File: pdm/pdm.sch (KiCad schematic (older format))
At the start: 29 parts, among them J1 Conn_01x05, J2 Conn_01x04_Male, SW1 SW_Push, U1 AZ1117CH-3_3TRG1, U2 SN65HVD233, U3 STM32F042G6Ux

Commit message: changed to molex headers
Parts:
- removed H6, H7: MountingHole_Pad, MountingHole:MountingHole_4mm_Pad_Via, symbol Mechanical:MountingHole_Pad
- removed J1: Conn_01x05, Connector_PinHeader_2.00mm:PinHeader_1x05_P2.00mm_Vertical, symbol Connector_Generic:Conn_01x05
- removed J2: Conn_01x04_Male, Connector_PinHeader_2.00mm:PinHeader_1x04_P2.00mm_Horizontal, symbol Connector:Conn_01x04_Male
- added CANH_Test1: CANH_TEST, TestPoint:TestPoint_Pad_D1.0mm, symbol Connector:TestPoint_Probe
- added CANL_Test1: CANL_TEST, TestPoint:TestPoint_Pad_D1.0mm, symbol Connector:TestPoint_Probe
- added J1: Conn_01x04_Male, Connector_Molex:Molex_Mega-Fit_76829-0004_2x02_P5.70mm_Vertical, symbol Connector:Conn_01x04_Male
- added J2: Conn_01x08_Male, Connector_Molex:Molex_Mega-Fit_76829-0008_2x04_P5.70mm_Vertical, symbol Connector:Conn_01x08_Male
- added TP11, TP12, TP?: TestPoint_Probe, TestPoint:TestPoint_Pad_D1.0mm, symbol Connector:TestPoint_Probe
- C1: renamed from C9; value 100nF -> 0.1uF; Digi-Key_PN (none) -> CL21B104KBCNNNC
- C2: renamed from C3; value 0.1 uF -> 0.1uF; Digi-Key_PN (none) -> CL21B104KBCNNNC
- C3: renamed from C2; value 0.1 uF -> 0.1uF; Digi-Key_PN (none) -> CL21B104KBCNNNC
- C4: renamed from C6; value 20p -> 20pF; Digi-Key_PN (none) -> 08051A200JAT2A
- C5: renamed from C4; value 20p -> 20pF; Digi-Key_PN (none) -> 08051A200JAT2A
- C6: renamed from C1; footprint Capacitor_SMD:CP_Elec_4x5.4 -> Capacitor_Tantalum_SMD:CP_EIA-3216-18_Kemet-A_Pad1.58x1.35mm_HandSolder
- C7: renamed from C5; value 100nF -> 0.1uF; Digi-Key_PN (none) -> CL21B104KBCNNNC
- C8: renamed from C15; Digi-Key_PN (none) -> T494A106M020AT
- C9: renamed from C7; value 100nF -> 0.1uF; Digi-Key_PN (none) -> CL21B104KBCNNNC
- renumbered C14 to C10, C8 to C11, D11 to D1, D12 to D2, D1 to D3, R33 to R1, R1 to R2, R34 to R3, R2 to R4, R23 to R5, R24 to R6
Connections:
- wire segments 118 -> 131
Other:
- note added: "Signal Connector"
- note removed: "CAN Bus checkup? Is that alright?\n\nCANH and CANL - is the only criteria for differential the fact \nthey have to be close?"
- note removed: "Double Check the 12V Blocks"
- note removed: "General Questions"
- note removed: "SWD Programmer"
- note removed: "SWD Setup"
- note removed: "use an onboard connector - eg. use a pcb deutche\nconnector foor this one (DTM Connector)"
- moved on the sheet: C11, C3, C6, D1, D2, R1, R3, U1

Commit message: changed layout with two plugs
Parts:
- removed C1: 0.1uF, Capacitor_SMD:C_0805_2012Metric_Pad1.15x1.40mm_HandSolder, symbol Device:C
- removed J2: Conn_01x08_Male, Connector_Molex:Molex_Mega-Fit_76829-0008_2x04_P5.70mm_Vertical, symbol Connector:Conn_01x08_Male
- removed R2: 1M, Resistor_SMD:R_0805_2012Metric_Pad1.15x1.40mm_HandSolder, symbol Device:R
- added J2: Conn_01x12_Male, DT13-12PB-B016:TE_DT13-12PB-B016, symbol Connector:Conn_01x12_Male
- added J3: Conn_01x08_Male, Connector_PinSocket_2.54mm:PinSocket_2x04_P2.54mm_Vertical_SMD, symbol Connector:Conn_01x08_Male
- added R2: 10K, Resistor_SMD:R_0805_2012Metric_Pad1.20x1.40mm_HandSolder, symbol pdm-rescue:R-Device
- C10, C2, C3, C4, C5, C7, C8, C9: footprint Capacitor_SMD:C_0805_2012Metric_Pad1.15x1.40mm_HandSolder -> Capacitor_SMD:C_0805_2012Metric_Pad1.18x1.45mm_HandSolder; symbol Device:C -> pdm-rescue:C-Device
- C11, C6: symbol Device:CP -> pdm-rescue:CP-Device
- CANH_Test1, CANL_Test1, TP11, TP12: symbol Connector:TestPoint_Probe -> pdm-rescue:TestPoint_Probe-Connector
- D1, D2, D3: symbol Device:LED -> pdm-rescue:LED-Device
- J1: footprint Connector_Molex:Molex_Mega-Fit_76829-0004_2x02_P5.70mm_Vertical -> DT13-4P:TE_DT13-4P
- R1, R3, R4, R5, R6: footprint Resistor_SMD:R_0805_2012Metric_Pad1.15x1.40mm_HandSolder -> Resistor_SMD:R_0805_2012Metric_Pad1.20x1.40mm_HandSolder; symbol Device:R -> pdm-rescue:R-Device
- SW1: symbol Switch:SW_Push -> pdm-rescue:SW_Push-Switch
- TP13: renamed from TP?; symbol Connector:TestPoint_Probe -> pdm-rescue:TestPoint_Probe-Connector
- U2: symbol Interface_CAN_LIN:SN65HVD233 -> pdm-rescue:SN65HVD233-Interface_CAN_LIN
- U3: symbol MCU_ST_STM32F0:STM32F042G6Ux -> pdm-rescue:STM32F042G6Ux-MCU_ST_STM32F0
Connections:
- net +12V: now also J1.3 (Pin_3), J1.4 (Pin_4); no longer J1.1 (Pin_1)
- net +3V3: now also U1.4 (VOUT), J2.1 (Pin_1), J3.6 (Pin_6), J3.7 (Pin_7); no longer U3.17 (VDD)
- net GND: now also J1.1 (Pin_1), J2.2 (Pin_2), J3.8 (Pin_8), R2.1; no longer J1.3 (Pin_3), J1.4 (Pin_4)
- net NRST: now also J3.3 (Pin_3), R2.2
- net SWCLK: now also J3.5 (Pin_5)
- net SWDIO: now also J3.4 (Pin_4)
- net _N: now also J2.11 (Pin_11), J3.1 (Pin_1)
- net _P: now also J2.12 (Pin_12), J3.2 (Pin_2)
- new net VDD: U3.17 (VDD)
- new net vout1: J2.10 (Pin_10), J2.3 (Pin_3)
- new net vout2: J2.4 (Pin_4), J2.9 (Pin_9)
- new net vout3: J2.5 (Pin_5), J2.8 (Pin_8)
- new net vout4: J2.6 (Pin_6)
- new net vout5: J2.7 (Pin_7)
- no-connect marks 1 -> 0
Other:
- moved on the sheet: C3, CANH_Test1, CANL_Test1, TP11, TP12, U3

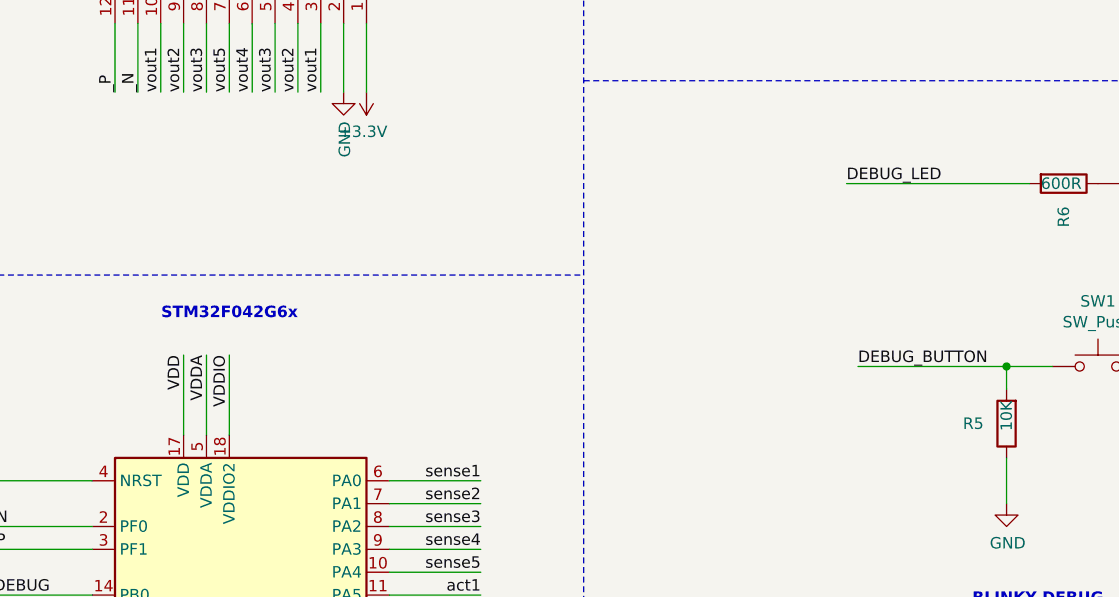
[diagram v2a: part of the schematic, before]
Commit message: added mounting holes again
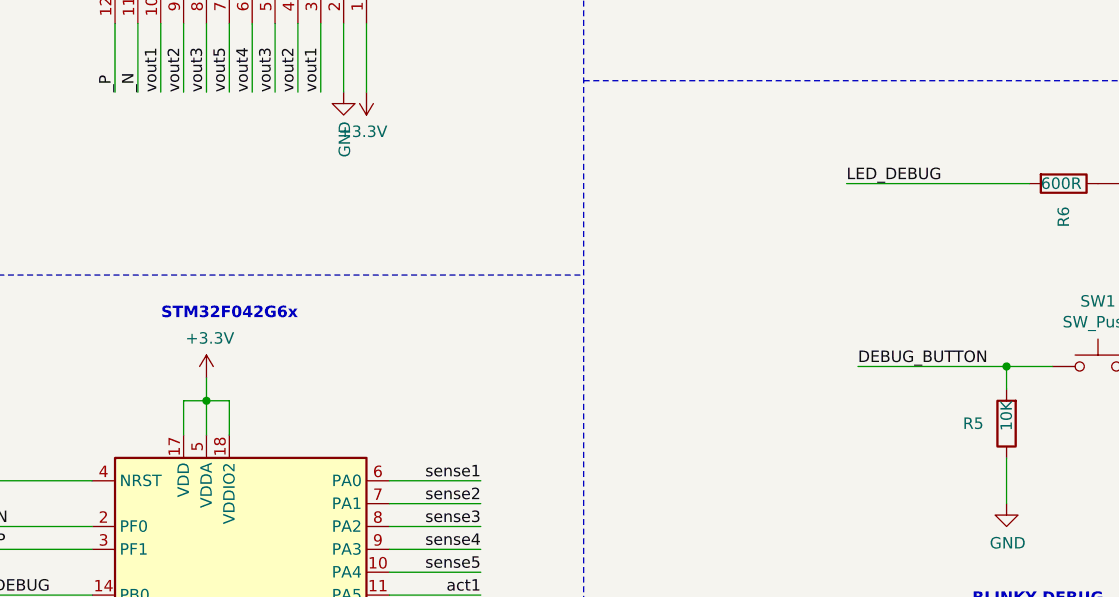
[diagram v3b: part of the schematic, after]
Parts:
- XTAL1: footprint digikey-footprints:SMD-2_3.2x2.5mm -> Oscillator:Oscillator_SMD_Abracon_ASE-4Pin_3.2x2.5mm
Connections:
- net DEBUG_LED is gone; now on net LED_DEBUG: R6.2
- net VDD is gone; now on net +3V3: U3.17 (VDD)
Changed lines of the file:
@@
 F 0 "XTAL1" H 1450 4440 50  0000 C CNN
 F 1 "NX3225GD-8MHZ-STD-CRA-3" H 1450 4349 50  0000 C CNN
-F 2 "digikey-footprints:SMD-2_3.2x2.5mm" H 1650 4400 60  0001 L CNN
+F 2 "Oscillator:Oscillator_SMD_Abracon_ASE-4Pin_3.2x2.5mm" H 1650 4400 60  0001 L CNN
 F 3 "http://www.ndk.com/images/products/catalog/c_NX3225GD-STD-CRA-3_e.pdf" H 1650 4500 60  0001 L CNN
 F 4 "644-1178-1-ND" H 1650 4600 60  0001 L CNN "Digi-Key_PN"
@@
 Text Label 4450 6900 0    50   ~ 0
 fuse5
-Wire Wire Line
-	5450 5600 5450 5250
-Wire Wire Line
-	5650 5250 5650 5600
 Text Notes 1300 5750 1    50   ~ 0
 VDD
@@
 Text Label 1500 5200 3    50   ~ 0
 VDDA
-Text Label 5550 5250 3    50   ~ 0
-VDDA
 $Comp
 L pdm-rescue:STM32F042G6Ux-MCU_ST_STM32F0 U3
@@
 	1    0    0    -1
 $EndComp
-Wire Wire Line
-	5550 5600 5550 5250
-Text Label 5450 5250 3    50   ~ 0
-VDD
-Text Label 5650 5250 3    50   ~ 0
-VDDIO
 $Comp
 L pdm-rescue:+3.3V-power #PWR010
@@
 DEBUG_BUTTON
 Text Label 8350 4500 0    50   ~ 0
-DEBUG_LED
+LED_DEBUG
 Wire Wire Line
 	8350 4500 9150 4500
@@
 	0    -1   -1   0
 $EndComp
+$Comp
+L pdm-rescue:+3.3V-power #PWR0104
+U 1 1 6057B65E
+P 5550 5350
+F 0 "#PWR0104" H 5550 5200 50  0001 C CNN
+F 1 "+3.3V" H 5565 5523 50  0000 C CNN
+F 2 "" H 5550 5350 50  0001 C CNN
+F 3 "" H 5550 5350 50  0001 C CNN
+	1    5550 5350
+	1    0    0    -1
+$EndComp
+Wire Wire Line
+	5550 5450 5450 5450
+Wire Wire Line
+	5450 5450 5450 5600
+Wire Wire Line
+	5550 5350 5550 5450
+Connection ~ 5550 5450
+Wire Wire Line
+	5550 5450 5550 5600
+Wire Wire Line
+	5550 5450 5650 5450
+Wire Wire Line
+	5650 5450 5650 5600
 $EndSCHEMATC

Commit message: fixed labelling
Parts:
- CANH_TP1: renamed from CANH_Test1; value CANH_TEST -> CANH_Test1
- CANL_Test1: value CANL_TEST -> CANL_TP
- renumbered TP11 to 3V3_TP1, TP12 to GND_TP1, TP13 to Vin_TP
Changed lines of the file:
@@
 AR Path="/5F956034/600062B0" Ref="TP?"  Part="1"
 AR Path="/5F9560D2/600062B0" Ref="TP?"  Part="1"
-AR Path="/600062B0" Ref="TP11"  Part="1"
-F 0 "TP11" H 9656 1501 50  0000 R CNN
+AR Path="/600062B0" Ref="3V3_TP1"  Part="1"
+F 0 "3V3_TP1" H 9656 1501 50  0000 R CNN
 F 1 "TestPoint_Probe" H 9656 1410 50  0000 R CNN
 F 2 "TestPoint:TestPoint_Pad_D1.0mm" H 9900 1400 50  0001 C CNN
@@
 AR Path="/5F956034/6001F6DE" Ref="TP?"  Part="1"
 AR Path="/5F9560D2/6001F6DE" Ref="TP?"  Part="1"
-AR Path="/6001F6DE" Ref="TP12"  Part="1"
-F 0 "TP12" H 9106 2151 50  0000 R CNN
+AR Path="/6001F6DE" Ref="GND_TP1"  Part="1"
+F 0 "GND_TP1" H 9106 2151 50  0000 R CNN
 F 1 "TestPoint_Probe" H 9106 2060 50  0000 R CNN
 F 2 "TestPoint:TestPoint_Pad_D1.0mm" H 9350 2050 50  0001 C CNN
@@
 AR Path="/5F956034/6002DB6D" Ref="TP?"  Part="1"
 AR Path="/5F9560D2/6002DB6D" Ref="TP?"  Part="1"
-AR Path="/6002DB6D" Ref="CANH_Test1"  Part="1"
-F 0 "CANH_Test1" V 9550 1300 50  0000 R CNN
-F 1 "CANH_TEST" V 9550 900 50  0000 R CNN
+AR Path="/6002DB6D" Ref="CANH_TP1"  Part="1"
+F 0 "CANH_TP1" V 9550 1500 50  0000 R CNN
+F 1 "CANH_Test1" V 9450 1500 50  0000 R CNN
 F 2 "TestPoint:TestPoint_Pad_D1.0mm" H 9700 1000 50  0001 C CNN
 F 3 "~" H 9700 1000 50  0001 C CNN
@@
 AR Path="/5F9560D2/6002ED89" Ref="TP?"  Part="1"
 AR Path="/6002ED89" Ref="CANL_Test1"  Part="1"
-F 0 "CANL_Test1" V 9550 1200 50  0000 R CNN
-F 1 "CANL_TEST" V 9550 800 50  0000 R CNN
+F 0 "CANL_Test1" V 9550 1400 50  0000 R CNN
+F 1 "CANL_TP" V 9650 1400 50  0000 R CNN
 F 2 "TestPoint:TestPoint_Pad_D1.0mm" H 9700 900 50  0001 C CNN
 F 3 "~" H 9700 900 50  0001 C CNN
@@
 AR Path="/5F956034/6005DA4C" Ref="TP?"  Part="1"
 AR Path="/5F9560D2/6005DA4C" Ref="TP?"  Part="1"
-AR Path="/6005DA4C" Ref="TP13"  Part="1"
-F 0 "TP13" H 1450 6950 50  0000 R CNN
+AR Path="/6005DA4C" Ref="Vin_TP"  Part="1"
+F 0 "Vin_TP" H 1450 6950 50  0000 R CNN
 F 1 "TestPoint_Probe" H 1800 6850 50  0000 R CNN
 F 2 "TestPoint:TestPoint_Pad_D1.0mm" H 1350 6850 50  0001 C CNN
